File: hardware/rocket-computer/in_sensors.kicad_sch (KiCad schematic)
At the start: 24 parts, among them J1 BM05B-SRSS-TB, U2 ISM6HG256XTR, U23 INA230AIRGTR, U27 TPS22810DRVR, U3 IIS2MDCTR, U4 BMP585

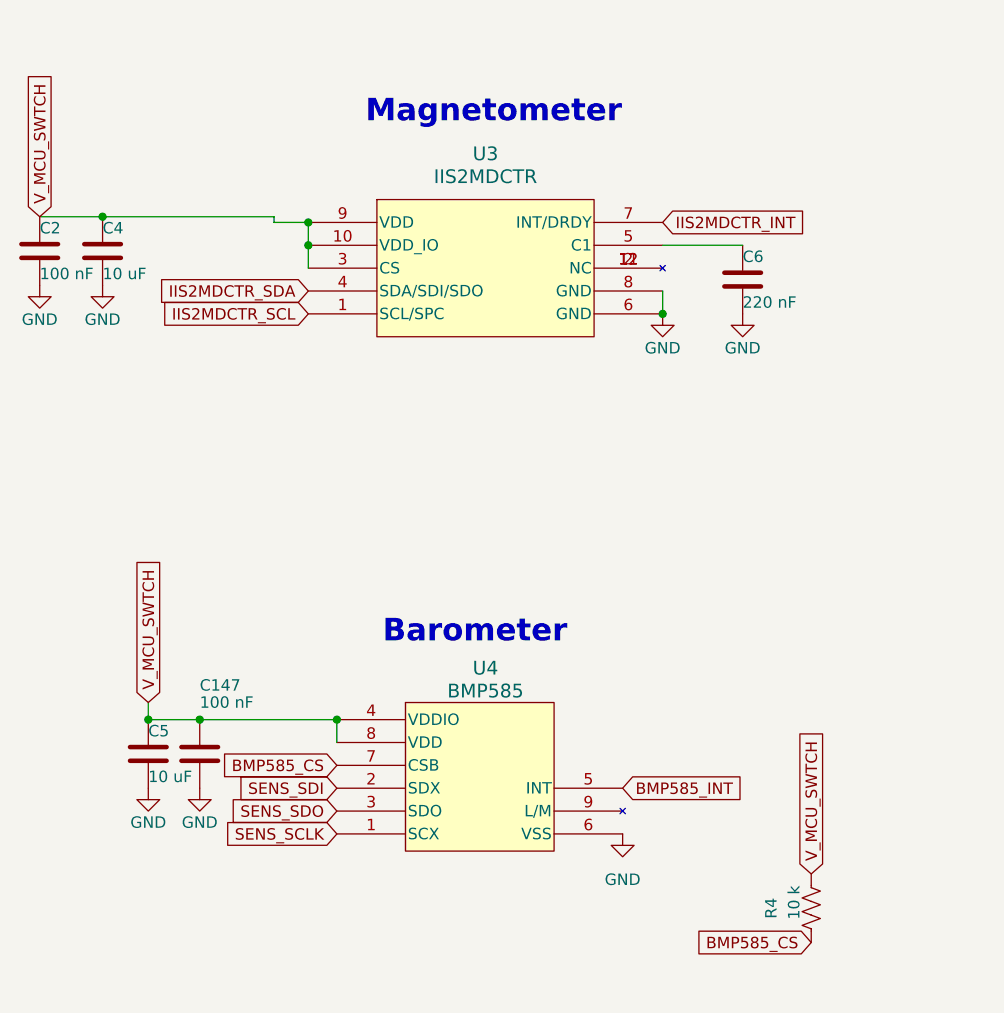
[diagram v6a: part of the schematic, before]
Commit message: hardware(V10): the part swaps the mini got and this board never did — both boot NORs, the pyro FETs, the magnetometer and the barometer (#1452)
v10-power-parity-2026-09-11.md closed the *circuit* differences between the
two boards, measuring forward from the TPS61094 rework (2026-08-29). It never
looked further back, and the *part* swaps in a4667604 (2026-08-16,
"hardware(minis): cost-reduction part swaps") only ever touched the two mini
boards. Two of that commit's six items had since arrived here by other routes
(DTC123JETL on 09-05, the PA0805 shunt); the rest had not.

Carried over:

- U13/U16 boot NOR: GD25Q128ESIG SOIC-8 208 mil -> W25Q128JVYIQ 24-ball WLCSP,
  the part the mini moved to on 2026-09-04. Both placements keep every net;
  only the pad names change (1-8 -> ball designators). Both blocks redrawn so
  the pins land on their labels, and U16's /CS pull-up R46 now runs over the
  top of the part into the VCC node.
- U6/U7/U8/U10 pyro high-side P-FETs: TPN4R712MD -> Winsok WSD20L50DN33. The
  incumbent is unbuyable at build quantity until the Q4-2026 Mouser restock;
  land compatibility was closed on the mini by numeric overlay of the vendor
  drawing. Same footprint, same 8-pin geometry, pins typed passive instead of
  unspecified.
- U9 pyro-ARM N-FET: CSD16323Q3 -> AOS AON7534. Same pinout, same land, and
  the mini keeps the CSD16323Q3 symbol for it, so this is fields only.
- U3 magnetometer: IIS2MDCTR LGA-12 2x2 -> QST QMC5883P LGA-16 3x3, with C6
  220 nF -> 10 uF for the C1 reservoir. Not pad-for-pad: IIS2MDCTR_SCL/SDA
  become MAG_SCL/MAG_SDA (the mini's names — they name the slot, not the part
  in it), the QMC land exposes no DRDY/INT pad so IIS2MDCTR_INT is gone and P4
  GPIO46 is free with a no-connect on it, and the ST part's separate VDD_IO and
  its CS strap to V_MCU_SWTCH go with it.
- U4 barometer: BMP585 LGA-9 -> BMP581 LGA-10 2x2. A drop-in on the drawing —
  the two symbols are built to the same pin grid, so U4 keeps its placement and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
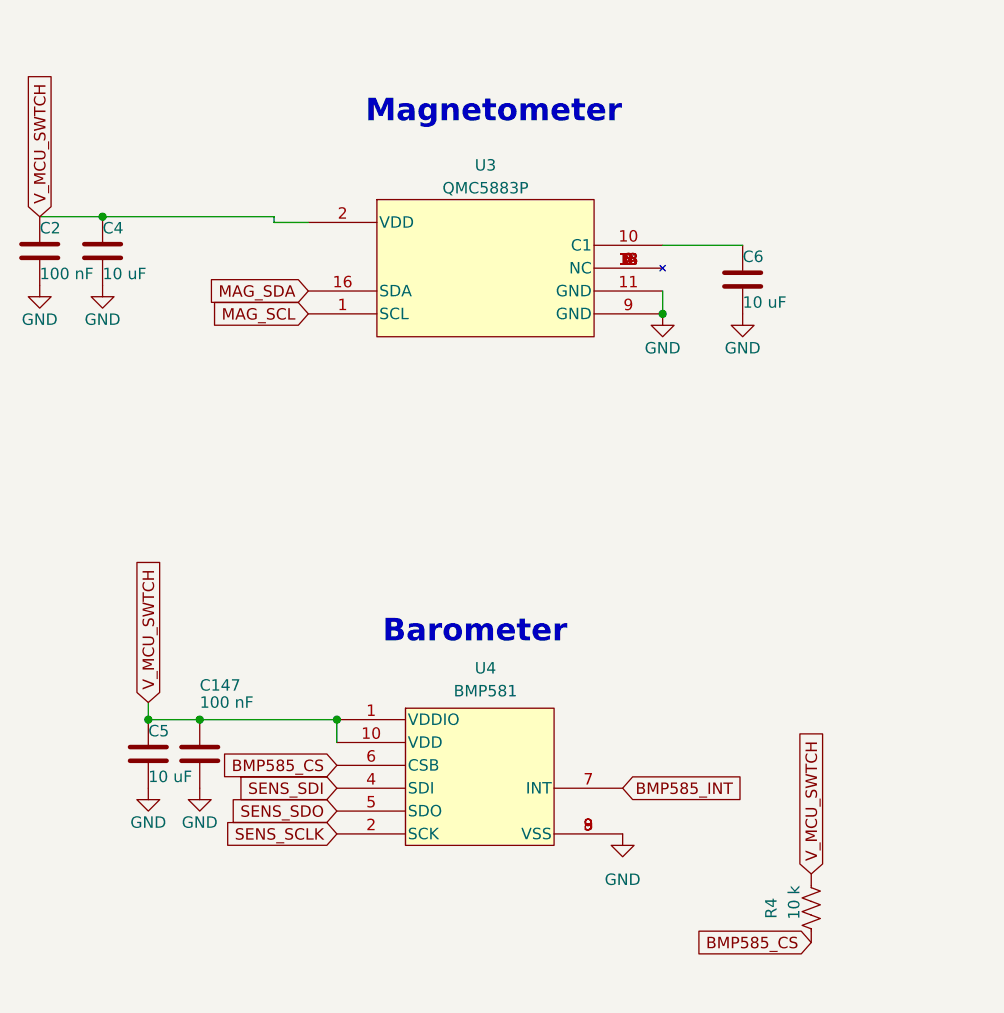
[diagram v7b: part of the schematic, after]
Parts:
- C6: value 220 nF -> 10 uF; MPN CL05B224KO5NNNC -> CL05A106MQ5NUNC
- C7: MPN CL21A226MOQNNNE -> CL21A226KOQNNNE
- U3: value IIS2MDCTR -> QMC5883P; footprint Footprints:LGA-12_2X2X0P7_STM -> Footprints:QMC5883P_LGA-16_3x3; symbol Custom:IIS2MDCTR -> Custom:QMC5883P; MPN IIS2MDCTR -> QMC5883P; Mfr STMicro -> QST
- U4: value BMP585 -> BMP581; footprint Footprints:LGA9_BMP585_BOS -> Footprints:BMP581_LGA-10_2x2; symbol Custom:BMP585 -> Custom:BMP581; MPN BMP585 -> BMP581
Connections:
- net IIS2MDCTR_SDA is gone; now on an unnamed net: U3.4 (NC)
- net BMP585_CS: now also U4.6 (CSB); no longer U4.7 (CSB)
- net BMP585_INT: now also U4.7 (INT); no longer U4.5 (INT)
- net GND: now also U3.11 (GND), U3.9 (GND), U4.3 (VSS), U4.8 (VSS), U4.9 (VSS); no longer U3.6 (GND), U3.8 (GND), U4.6 (VSS)
- net SENS_SCLK: now also U4.2 (SCK); no longer U4.1 (SCX)
- net SENS_SDI: now also U4.4 (SDI); no longer U4.2 (SDX)
- net SENS_SDO: now also U4.5 (SDO); no longer U4.3 (SDO)
- net V_MCU_SWTCH: now also U3.2 (VDD), U4.1 (VDDIO), U4.10 (VDD); no longer U3.10 (VDD_IO), U3.3 (CS), U3.9 (VDD), U4.4 (VDDIO), U4.8 (VDD)
- net at C6.1: now also U3.10 (C1); no longer U3.5 (C1)
- net IIS2MDCTR_INT: no longer names the net of U3.7 (NC)
- net IIS2MDCTR_INT: now also U3.12 (NC), U3.13 (NC), U3.14 (NC), U3.15 (NC), U3.3 (NC), U3.5 (NC), U3.6 (NC), U3.8 (NC)
- net IIS2MDCTR_SCL renamed MAG_SCL
- new net MAG_SDA: U3.16 (SDA)
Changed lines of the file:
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@@
 	)
 	(junction
-		(at 46.355 41.91)
-		(diameter 0)
-		(color 0 0 0 0)
-	)
-	(junction
 		(at 23.495 41.275)
 		(diameter 0)
@@
 	)
 	(junction
-		(at 46.355 44.45)
-		(diameter 0)
-		(color 0 0 0 0)
-	)
-	(junction
 		(at 28.575 97.155)
 		(diameter 0)
@@
 	(wire
 		(pts
-			(xy 46.355 41.91) (xy 46.355 44.45)
-		)
-		(stroke
-			(width 0)
-			(type default)
-		)
-	)
-	(wire
-		(pts
 			(xy 88.265 165.1) (xy 88.265 167.64)
 		)
@@
 	(wire
 		(pts
-			(xy 46.355 44.45) (xy 46.355 46.99)
-		)
-		(stroke
-			(width 0)
-			(type default)
-		)
-	)
-	(wire
-		(pts
 			(xy 85.725 49.53) (xy 85.725 52.07)
 		)
@@
 		)
 	)
-	(global_label "IIS2MDCTR_INT"
-		(shape input)
-		(at 85.725 41.91 0)
-		(fields_autoplaced yes)
-		(effects
-			(font
-				(size 1.27 1.27)
-			)
-			(justify left)
-		)
-		(property "Intersheetrefs" "${INTERSHEET_REFS}"
-			(at 102.4383 41.91 0)
-			(hide yes)
-			(show_name no)
-			(do_not_autoplace no)
-			(effects
-				(font
-					(size 1.27 1.27)
-				)
-				(justify left)
-			)
-		)
-	)
 	(global_label "V_MCU_SWTCH"
 		(shape input)
@@
 		)
 	)
-	(global_label "IIS2MDCTR_SDA"
+	(global_label "MAG_SDA"
 		(shape input)
 		(at 46.355 49.53 180)
@@
 		)
 	)
-	(global_label "IIS2MDCTR_SCL"
+	(global_label "MAG_SCL"
 		(shape input)
 		(at 46.355 52.07 180)
@@
 			)
 		)
-		(property "Value" "220 nF"
+		(property "Value" "10 uF"
 			(at 94.615 50.8 0)
 			(show_name no)
@@
 			)
 		)
-		(property "MPN" "CL05B224KO5NNNC"
+		(property "MPN" "CL05A106MQ5NUNC"
 			(at 94.615 48.26 0)
 			(hide yes)
@@
 			)
 		)
-		(property "MPN" "CL21A226MOQNNNE"
+		(property "MPN" "CL21A226KOQNNNE"
 			(at 182.88 43.815 0)
 			(hide yes)
@@
 		)
 	)
-	(symbol
-		(lib_id "Custom:IIS2MDCTR")
+		(symbol
+		(lib_id "Custom:QMC5883P")
 		(at 65.405 45.72 0)
 		(unit 1)
@@
 		(in_pos_files yes)
 		(dnp no)
-		(fields_autoplaced yes)
 		(property "Reference" "U3"
-			(at 66.04 34.29 0)
+			(at 66.04 35.56 0)
 			(show_name no)
 			(do_not_autoplace no)
 			(effects
 				(font
-					(size 1.524 1.524)
+					(size 1.27 1.27)
 				)
 			)
 		)
-		(property "Value" "IIS2MDCTR"
-			(at 66.04 36.83 0)
+		(property "Value" "QMC5883P"
+			(at 66.04 38.1 0)
 			(show_name no)
 			(do_not_autoplace no)
 			(effects
 				(font
-					(size 1.524 1.524)
+					(size 1.27 1.27)
 				)
 			)
 		)
-		(property "Footprint" "Footprints:LGA-12_2X2X0P7_STM"
+		(property "Footprint" "Footprints:QMC5883P_LGA-16_3x3"
 			(at 79.883 31.496 0)
 			(hide yes)
@@
 				(font
 					(size 1.27 1.27)
-					(italic yes)
 				)
 			)
 		)
-		(property "Datasheet" "https://www.st.com/resource/en/datasheet/iis2mdc.pdf"
+		(property "Datasheet" "QMC5883P"
 			(at 76.073 28.956 0)
 			(hide yes)
@@
 				(font
 					(size 1.27 1.27)
-					(italic yes)
 				)
 			)
@@
 			)
 		)
-		(property "MPN" "IIS2MDCTR"
+		(property "MPN" "QMC5883P"
 			(at 65.405 45.72 0)
 			(hide yes)
@@
 			)
 		)
-		(property "Mfr" "STMicro"
+		(property "Mfr" "QST"
 			(at 65.405 45.72 0)
 			(hide yes)
@@
 			)
 		)
-		(pin "2"
+		(pin "1"
 		)
-		(pin "5"
+		(pin "16"
 		)
-		(pin "11"
+		(pin "2"
 		)
-		(pin "12"
+		(pin "10"
 		)
 		(pin "9"
 		)
-		(pin "1"
+		(pin "11"
 		)
-		(pin "7"
+		(pin "3"
+		)
+		(pin "4"
+		)
+		(pin "5"
 		)
 		(pin "6"
 		)
+		(pin "7"
+		)
 		(pin "8"
 		)
-		(pin "4"
+		(pin "12"
 		)
-		(pin "3"
+		(pin "13"
 		)
-		(pin "10"
+		(pin "14"
+		)
+		(pin "15"
 		)
 		(instances
@@
 		)
 	)
-	(symbol
-		(lib_id "Custom:BMP585")
+		(symbol
+		(lib_id "Custom:BMP581")
 		(at 66.04 102.235 0)
 		(unit 1)
@@
 			(effects
 				(font
-					(size 1.524 1.524)
+					(size 1.27 1.27)
 				)
 			)
 		)
-		(property "Value" "BMP585"
+		(property "Value" "BMP581"
 			(at 66.04 93.98 0)
 			(show_name no)
@@
 			(effects
 				(font
-					(size 1.524 1.524)
+					(size 1.27 1.27)
 				)
 			)
 		)
-		(property "Footprint" "Footprints:LGA9_BMP585_BOS"
+		(property "Footprint" "Footprints:BMP581_LGA-10_2x2"
 			(at 66.04 102.235 0)
 			(hide yes)
@@
 				(font
 					(size 1.27 1.27)
-					(italic yes)
 				)
 			)
 		)
-		(property "Datasheet" "BMP585"
+		(property "Datasheet" "BMP581"
 			(at 66.04 102.235 0)
 			(hide yes)
@@
 				(font
 					(size 1.27 1.27)
-					(italic yes)
 				)
 			)
@@
 			)
 		)
-		(property "MPN" "BMP585"
+		(property "MPN" "BMP581"
 			(at 66.04 102.235 0)
 			(hide yes)
@@
 			)
 		)
-		(pin "4"
+		(pin "2"
 		)
-		(pin "3"
+		(pin "5"
+		)
+		(pin "4"
 		)
 		(pin "6"
 		)
-		(pin "5"
+		(pin "10"
 		)
 		(pin "1"
 		)
-		(pin "2"
+		(pin "7"
 		)
-		(pin "9"
+		(pin "3"
 		)
 		(pin "8"
 		)
-		(pin "7"
+		(pin "9"
 		)
 		(instances

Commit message: hardware(V10): the 22 uF 0805 goes back to the M-code, which is the grade the fleet actually buys
3ce1d38d moved the V10's twelve 22 uF 0805 from CL21A226MOQNNNE to
CL21A226KOQNNNE on the grounds that the mini uses the K grade. The mini does,
in its schematic — but the priced CrossBoard BOM retired that line on
2026-08-28 and merged both minis back onto the M-code, because the K repriced
UP to $0.1257@2000 while the M-code sibling sells at $0.0725. So the parity
argument was reading a stale source: the sourcing decision had already gone the
other way, and nothing anywhere claims the K's tighter +/-10% tolerance is
needed at any of these sites.

All twelve placements (C7, C8, C9, C10, C11, C13, C14, C17, C18, C43, C141,
C144) revert to CL21A226MOQNNNE — same Samsung series, same 0805, same 16 V,
which is what the >=16 V requirement on the 2S rails asks for. Ten of the
twelve are placed on the board and take the field change there too; C141 and
C144 are among the parts still waiting to be placed.

Note for whoever next touches the mini: its schematic is now the odd one out
and should follow the same way.

Measured: field-only change. Netlist component count unchanged at 277, every
net identical. kicad-cli pcb drc --severity-all --schematic-parity unchanged at
162 violations and 97 parity items. bom.csv regenerated and reconciled to the
schematic across all 265 designators. check_docs.py clean.

Co-Authored-By: Claude Opus 5 <noreply@anthropic.com>
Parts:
- C7: MPN CL21A226KOQNNNE -> CL21A226MOQNNNE
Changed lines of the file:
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@@
 			)
 		)
-		(property "MPN" "CL21A226KOQNNNE"
+		(property "MPN" "CL21A226MOQNNNE"
 			(at 182.88 43.815 0)
 			(hide yes)
